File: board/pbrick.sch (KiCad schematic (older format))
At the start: 51 parts, among them J1 S8B-PH-SM4-TB_LF__SN_, J2 UJC-HP-3-SMT-TR, J3 QWIIC, J5 U.FL2PIN, P1 SWD, Q1 SSM6J507NU, Q2 SSM6J507NU, U1 TB67H420FTG(O,EL), U2 MIC5219-3.3YML-TR, U3 ADP3330ARTZ-5-RL7, U4 STUSB4500QTR

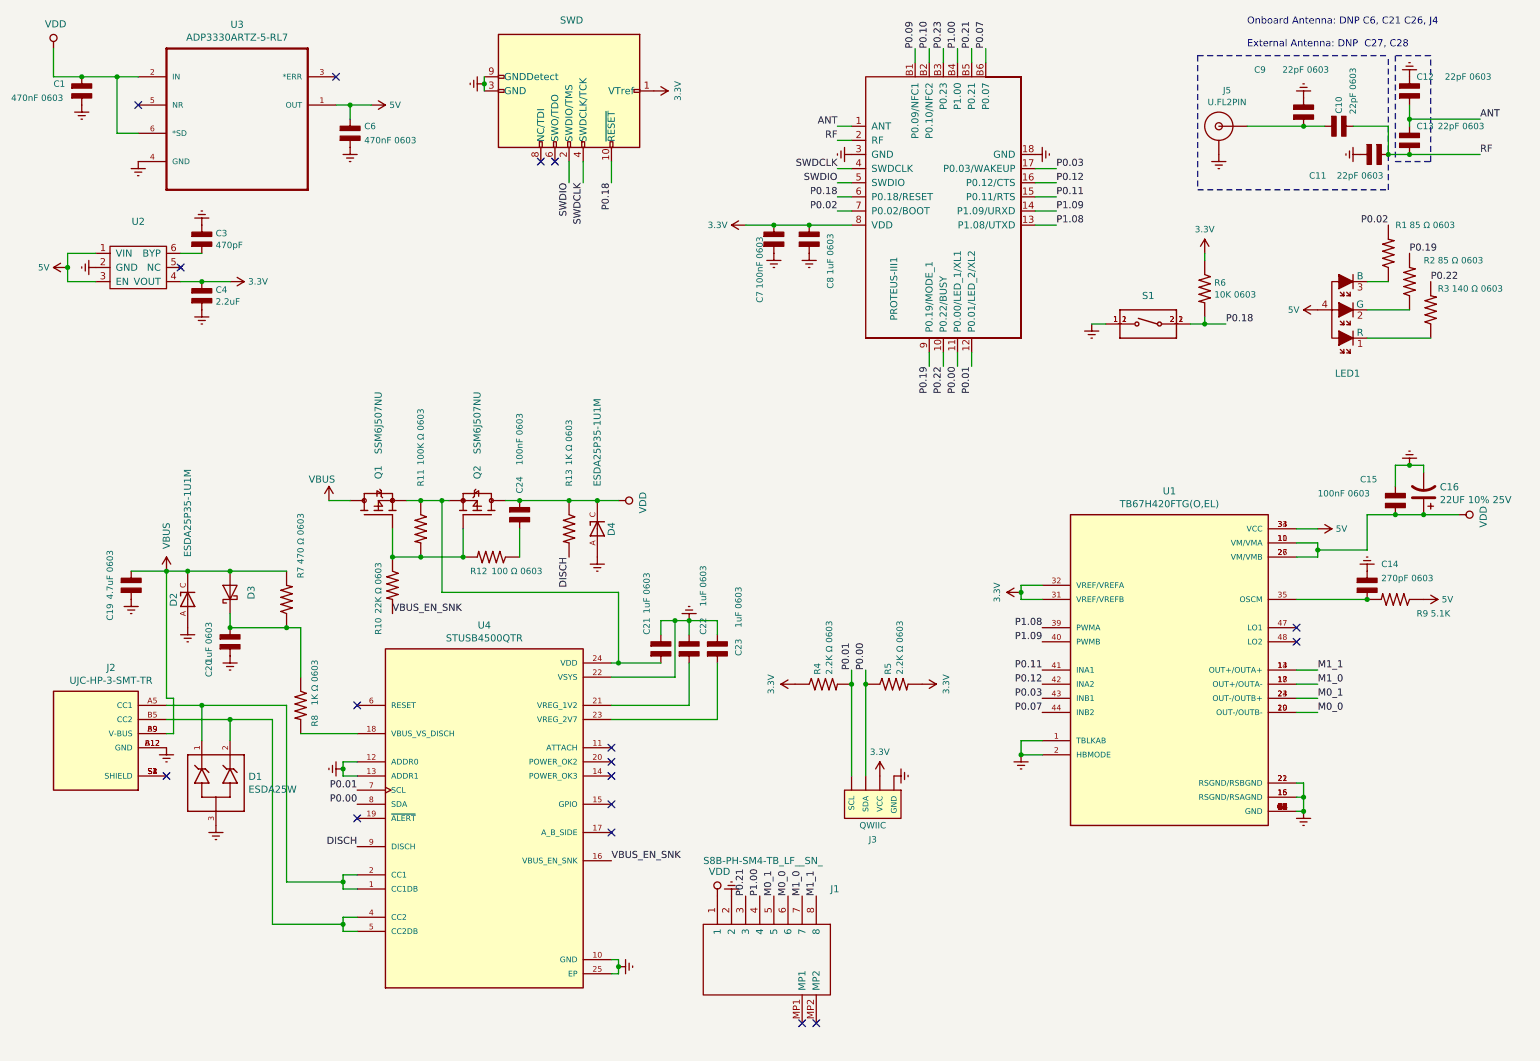
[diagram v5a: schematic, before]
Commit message: Adding new symbols
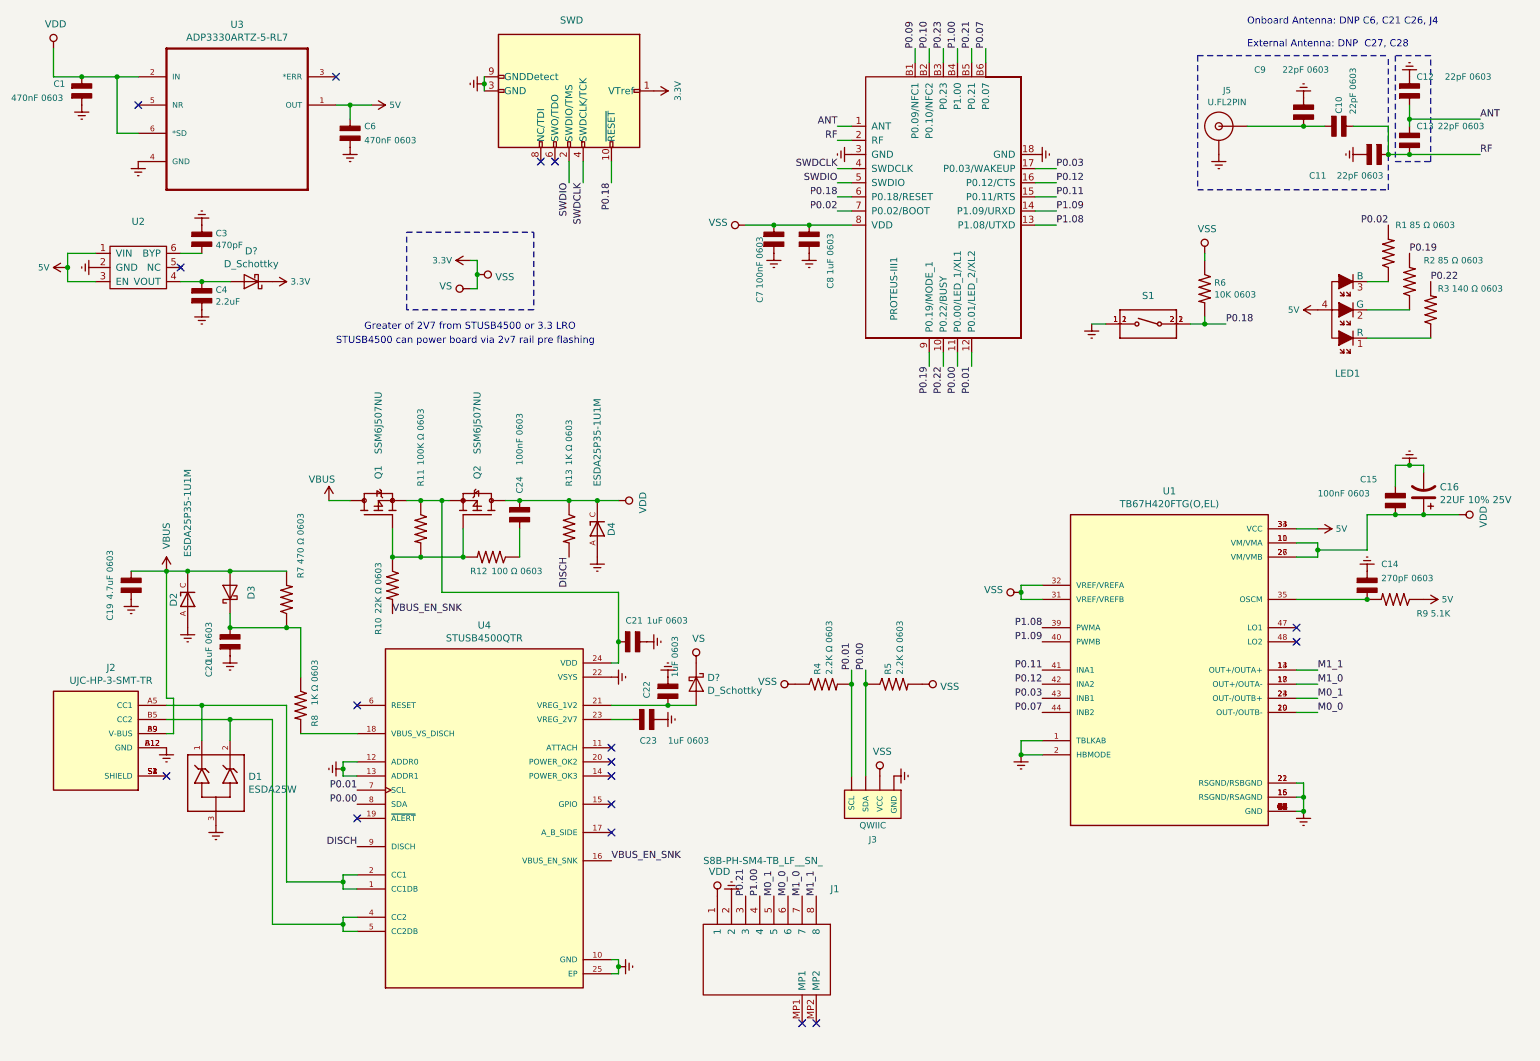
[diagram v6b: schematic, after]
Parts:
- added D? (x2): D_Schottky, Diode_SMD:D_0402_1005Metric, symbol Device:D_Schottky
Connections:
- net 3.3V: now also D?.1 (K), D?.1 (K); no longer C4.1, U2.4 (VOUT)
- net at C22.2, U4.21 (VREG_1V2): now also D?.2 (A)
- new net: C4.1, D?.2 (A), U2.4 (VOUT)
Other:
- note added: "Greater of 2V7 from STUSB4500 or 3.3 LRO\n"
- note added: "STUSB4500 can power board via 2v7 rail pre flashing"
- moved on the sheet: C21, C22, C23

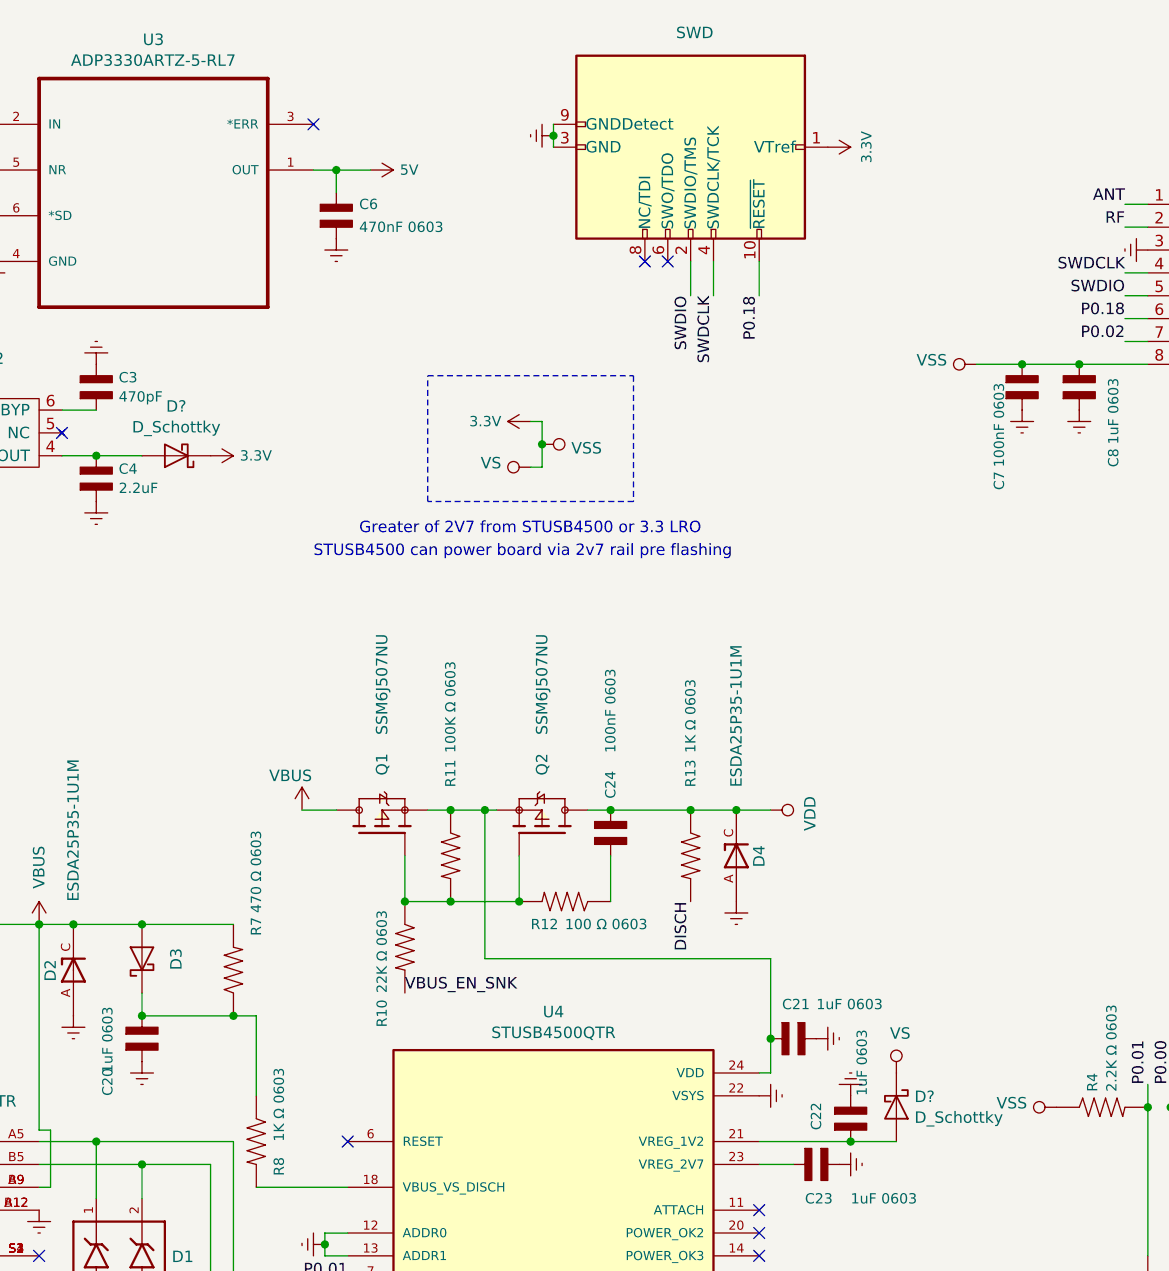
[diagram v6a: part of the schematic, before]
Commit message: TD2030 pin connector instead of CotexDebug, routable path
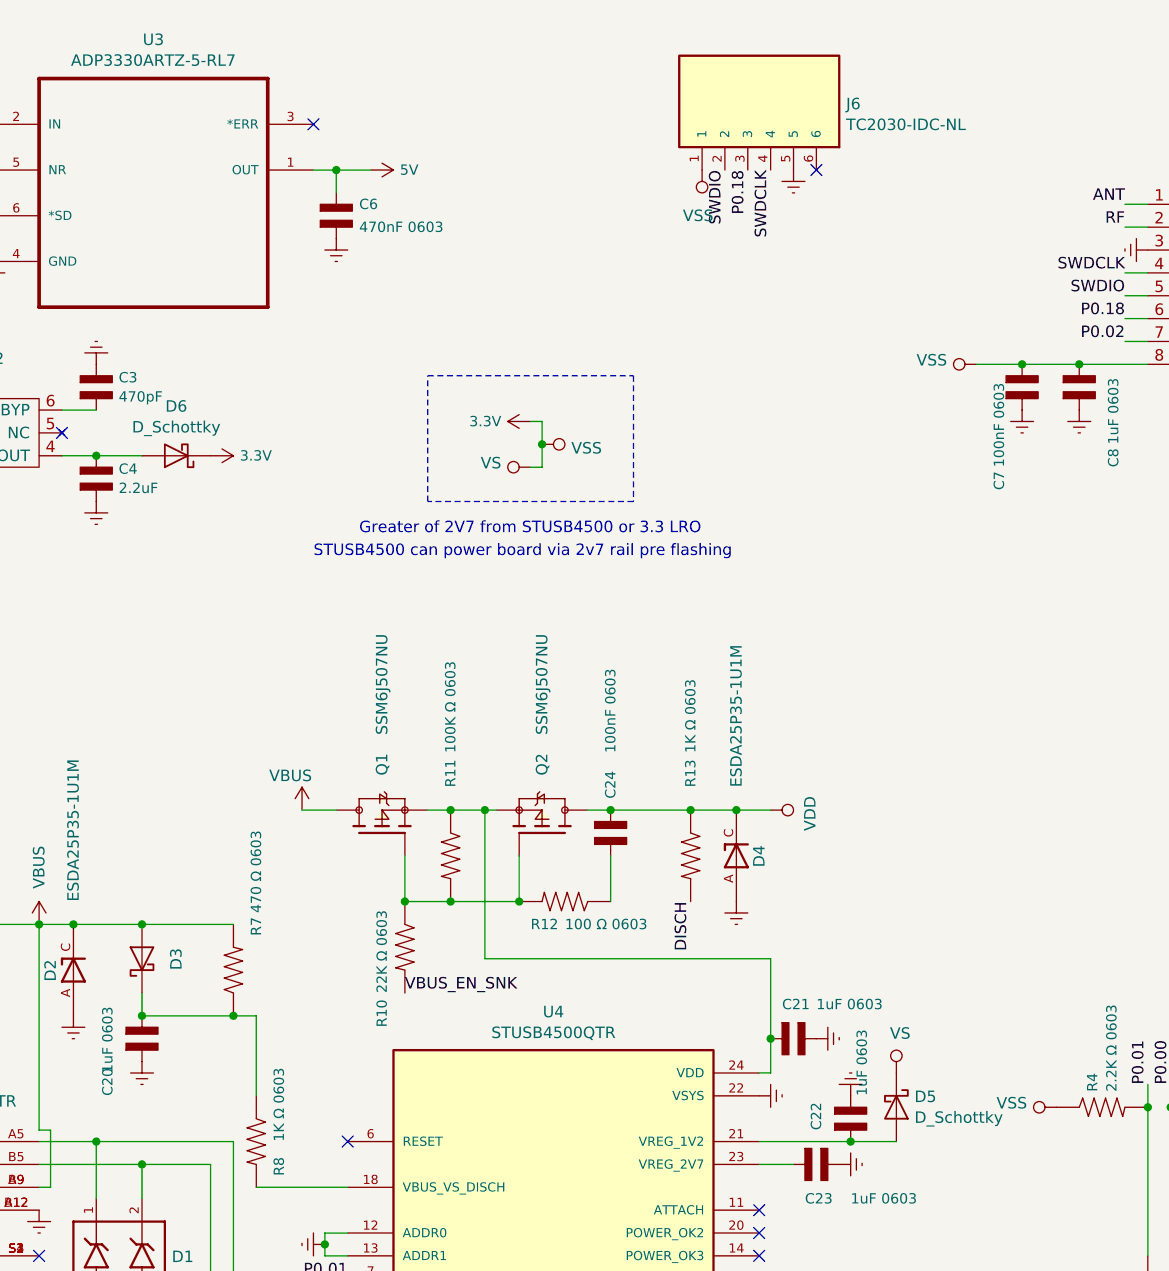
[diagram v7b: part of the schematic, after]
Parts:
- removed P1: SWD, Connectors:SAMTECH_FTSH-105-01, symbol Connector:Conn_ARM_JTAG_SWD_10
- added J6: TC2030-IDC-NL, TAG_TC2030-IDC-NL, symbol TC2030-IDC-NL:TC2030-IDC-NL
- gave numbers to parts that had none: 2
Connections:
- net 3.3V: now also J6.1
- net Earth: now also J6.5
- net P0.18: now also J6.3
- net SWDCLK: now also J6.4
- net SWDIO: now also J6.2
- no-connect marks 17 -> 16
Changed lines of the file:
@@
 Wire Wire Line
 	9000 2800 9150 2800
-Text Label 4800 1800 3    50   ~ 0
+Text Label 4750 1250 3    50   ~ 0
 P0.18
 Text Label 6400 1700 2    50   ~ 0
 SWDCLK
-Text Label 4600 1800 3    50   ~ 0
+Text Label 4850 1250 3    50   ~ 0
 SWDCLK
-Text Label 4500 1800 3    50   ~ 0
+Text Label 4650 1250 3    50   ~ 0
 SWDIO
-$Comp
-L pbrick-rescue:3.3V-SparkFun-PowerSymbols #SUPPLY011
-U 1 1 5F10E31F
-P 5100 1150
-F 0 "#SUPPLY011" H 5150 1150 45  0001 L BNN
-F 1 "3.3V" H 5100 1320 45  0000 C CNN
-F 2 "XXX-00000" V 5058 1277 60  0001 L CNN
-F 3 "" H 5100 1150 60  0001 C CNN
-	1    5100 1150
-	0    1    1    0
-$EndComp
-Wire Wire Line
-	3900 1050 3900 1100
-NoConn ~ 4400 1650
-NoConn ~ 4300 1650
-Wire Wire Line
-	4800 1650 4800 1800
-Wire Wire Line
-	4600 1800 4600 1650
-Wire Wire Line
-	4500 1650 4500 1800
+NoConn ~ 5050 1250
 $Comp
 L power:Earth #PWR020
 U 1 1 5F110ED4
-P 3900 1100
-F 0 "#PWR020" H 3900 850 50  0001 C CNN
-F 1 "Earth" H 3900 950 50  0001 C CNN
-F 2 "" H 3900 1100 50  0001 C CNN
-F 3 "~" H 3900 1100 50  0001 C CNN
-	1    3900 1100
-	0    1    1    0
-$EndComp
-Connection ~ 3900 1100
-Wire Wire Line
-	3900 1100 3900 1150
+P 4950 1250
+F 0 "#PWR020" H 4950 1000 50  0001 C CNN
+F 1 "Earth" H 4950 1100 50  0001 C CNN
+F 2 "" H 4950 1250 50  0001 C CNN
+F 3 "~" H 4950 1250 50  0001 C CNN
+	1    4950 1250
+	1    0    0    -1
+$EndComp
 $Comp
 L power:Earth #PWR022
@@
 	6600 5350 6600 5250
 Connection ~ 6600 5350
-$Comp
-L Connector:Conn_ARM_JTAG_SWD_10 P1
-U 1 1 5F109E09
-P 4500 1150
-F 0 "P1" V 4200 1600 50  0001 R CNN
-F 1 "SWD" V 4000 1250 50  0000 R CNN
-F 2 "Connectors:SAMTECH_FTSH-105-01" H 4500 1150 50  0001 C CNN
-F 3 "http://infocenter.arm.com/help/topic/com.arm.doc.ddi0314h/DDI0314H_coresight_components_trm.pdf" V 4150 -100 50  0001 C CNN
-F 4 "dnp" V 4500 1150 50  0001 C CNN "fit_field"
-	1    4500 1150
-	0    1    1    0
-$EndComp
 $Comp
 L pbrick-rescue:150121M153000-150121M153000 LED1
@@
 	3600 4050 3450 4050
 $Comp
-L Device:D_Schottky D?
+L Device:D_Schottky D5
 U 1 1 60193B83
 P 5400 5350
-F 0 "D?" V 5354 5429 50  0000 L CNN
+F 0 "D5" V 5354 5429 50  0000 L CNN
 F 1 "D_Schottky" V 5445 5429 50  0000 L CNN
 F 2 "Diode_SMD:D_0402_1005Metric" H 5400 5350 50  0001 C CNN
@@
 $EndComp
 $Comp
-L Device:D_Schottky D?
+L Device:D_Schottky D6
 U 1 1 601C167B
 P 2250 2500
-F 0 "D?" H 2250 2284 50  0000 C CNN
+F 0 "D6" H 2250 2284 50  0000 C CNN
 F 1 "D_Schottky" H 2250 2375 50  0000 C CNN
 F 2 "Diode_SMD:D_0402_1005Metric" H 2250 2500 50  0001 C CNN
@@
 Text Notes 2850 2950 0    50   ~ 0
 STUSB4500 can power board via 2v7 rail pre flashing
+$Comp
+L TC2030-IDC-NL:TC2030-IDC-NL J6
+U 1 1 601985D5
+P 4850 950
+F 0 "J6" V 4839 620 50  0000 R CNN
+F 1 "TC2030-IDC-NL" V 4748 620 50  0000 R CNN
+F 2 "TAG_TC2030-IDC-NL" H 4850 950 50  0001 L BNN
+F 3 "" H 4850 950 50  0001 L BNN
+F 4 "MS" H 4850 950 50  0001 L BNN "PARTREV"
+F 5 "Tag-Connect" H 4850 950 50  0001 L BNN "MANUFACTURER"
+F 6 "Manufacturer recommendation" H 4850 950 50  0001 L BNN "STANDARD"
+	1    4850 950
+	0    -1   -1   0
+$EndComp
+$Comp
+L power:VSS #PWR?
+U 1 1 601995E8
+P 4550 1250
+F 0 "#PWR?" H 4550 1100 50  0001 C CNN
+F 1 "VSS" H 4500 1450 50  0000 L CNN
+F 2 "" H 4550 1250 50  0001 C CNN
+F 3 "" H 4550 1250 50  0001 C CNN
+	1    4550 1250
+	-1   0    0    1
+$EndComp
 $EndSCHEMATC
